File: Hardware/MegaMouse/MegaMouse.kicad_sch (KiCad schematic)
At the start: 7 parts, among them J101 MotorL, J102 MotorR, U101 ATmega328P-A, U102 HDSP-7803

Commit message: Make awesome
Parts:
- removed J101: MotorL, MegaMouse:MicroMotor, symbol Connector:Conn_01x05_Female
- removed J102: MotorR, MegaMouse:MicroMotor, symbol Connector:Conn_01x05_Female
- added BT102: Cell2, Battery:BatteryHolder_MPD_BH-18650-PC2, symbol Device:Battery_Cell
- BT101: value Battery_Cell -> Cell1
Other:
- added sheet LeftMotor (motor.kicad_sch)
- added sheet RightMotor (motor.kicad_sch)
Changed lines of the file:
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@@
       (effects (font (size 1.27 1.27)) (justify left))
     )
-    (property "Value" "Battery_Cell" (id 1) (at 238.76 48.7679 0)
+    (property "Value" "Cell1" (id 1) (at 238.76 48.7679 0)
       (effects (font (size 1.27 1.27)) (justify left))
     )
@@
     (pin "3")
   )
-  (symbol (lib_id "Connector:Conn_01x05_Female") (at 205.74 85.725 0) (unit 1)
-    (in_bom yes) (on_board yes) (fields_autoplaced)
-    (property "Reference" "J101" (id 0) (at 207.01 84.4549 0)
-      (effects (font (size 1.27 1.27)) (justify left))
-    )
-    (property "Value" "MotorL" (id 1) (at 207.01 86.9949 0)
-      (effects (font (size 1.27 1.27)) (justify left))
-    )
-    (property "Footprint" "MegaMouse:MicroMotor" (id 2) (at 205.74 85.725 0)
-      (effects (font (size 1.27 1.27)) hide)
-    )
-    (property "Datasheet" "~" (id 3) (at 205.74 85.725 0)
-      (effects (font (size 1.27 1.27)) hide)
-    )
-    (pin "1")
-    (pin "2")
-    (pin "3")
-    (pin "4")
-    (pin "5")
-  )
   (symbol (lib_id "Device:LED_Dual_AAK") (at 43.815 74.93 0) (unit 1)
     (in_bom yes) (on_board yes) (fields_autoplaced)
@@
     (pin "3")
   )
-  (symbol (lib_id "Connector:Conn_01x05_Female") (at 222.25 85.725 0) (unit 1)
-    (in_bom yes) (on_board yes) (fields_autoplaced)
-    (property "Reference" "J102" (id 0) (at 223.52 84.4549 0)
-      (effects (font (size 1.27 1.27)) (justify left))
-    )
-    (property "Value" "MotorR" (id 1) (at 223.52 86.9949 0)
-      (effects (font (size 1.27 1.27)) (justify left))
-    )
-    (property "Footprint" "MegaMouse:MicroMotor" (id 2) (at 222.25 85.725 0)
-      (effects (font (size 1.27 1.27)) hide)
-    )
-    (property "Datasheet" "~" (id 3) (at 222.25 85.725 0)
-      (effects (font (size 1.27 1.27)) hide)
-    )
-    (pin "1")
-    (pin "2")
-    (pin "3")
-    (pin "4")
-    (pin "5")
+  (symbol (lib_id "Device:Battery_Cell") (at 250.19 49.53 0) (unit 1)
+    (in_bom yes) (on_board yes) (fields_autoplaced)
+    (property "Reference" "BT102" (id 0) (at 254 46.2279 0)
+      (effects (font (size 1.27 1.27)) (justify left))
+    )
+    (property "Value" "Cell2" (id 1) (at 254 48.7679 0)
+      (effects (font (size 1.27 1.27)) (justify left))
+    )
+    (property "Footprint" "Battery:BatteryHolder_MPD_BH-18650-PC2" (id 2) (at 250.19 48.006 90)
+      (effects (font (size 1.27 1.27)) hide)
+    )
+    (property "Datasheet" "~" (id 3) (at 250.19 48.006 90)
+      (effects (font (size 1.27 1.27)) hide)
+    )
+    (pin "1")
+    (pin "2")
+  )
+  (sheet (at 245.745 60.325) (size 33.02 19.05) (fields_autoplaced)
+    (stroke (width 0.1524) (type solid) (color 0 0 0 0))
+    (fill (color 0 0 0 0.0000))
+    (property "Sheet name" "LeftMotor" (id 0) (at 245.745 59.6134 0)
+      (effects (font (size 1.27 1.27)) (justify left bottom))
+    )
+    (property "Sheet file" "motor.kicad_sch" (id 1) (at 245.745 79.9596 0)
+      (effects (font (size 1.27 1.27)) (justify left top))
+    )
+  )
+  (sheet (at 245.745 87.63) (size 33.02 19.05) (fields_autoplaced)
+    (stroke (width 0.1524) (type solid) (color 0 0 0 0))
+    (fill (color 0 0 0 0.0000))
+    (property "Sheet name" "RightMotor" (id 0) (at 245.745 86.9184 0)
+      (effects (font (size 1.27 1.27)) (justify left bottom))
+    )
+    (property "Sheet file" "motor.kicad_sch" (id 1) (at 245.745 107.2646 0)
+      (effects (font (size 1.27 1.27)) (justify left top))
+    )
   )
   (sheet_instances
     (path "/" (page "1"))
+    (path "/cab2ae08-2794-43d3-b90a-39adfeeefd96" (page "2"))
+    (path "/f3134389-3b86-403d-ae8e-c46efd53e738" (page "3"))
   )
   (symbol_instances
@@
       (reference "#PWR0101") (unit 1) (value "GND") (footprint "")
     )
+    (path "/cab2ae08-2794-43d3-b90a-39adfeeefd96/30939476-66e6-4fc1-980c-82ef7e0fb2a1"
+      (reference "#PWR0102") (unit 1) (value "GND") (footprint "")
+    )
+    (path "/cab2ae08-2794-43d3-b90a-39adfeeefd96/1459ec6e-ec07-4a49-921b-662925b52015"
+      (reference "#PWR0103") (unit 1) (value "GND") (footprint "")
+    )
+    (path "/cab2ae08-2794-43d3-b90a-39adfeeefd96/4f63fd2b-66dc-4283-9050-d0dcbca9f9c1"
+      (reference "#PWR0104") (unit 1) (value "+5V") (footprint "")
+    )
+    (path "/f3134389-3b86-403d-ae8e-c46efd53e738/30939476-66e6-4fc1-980c-82ef7e0fb2a1"
+      (reference "#PWR0105") (unit 1) (value "GND") (footprint "")
+    )
+    (path "/f3134389-3b86-403d-ae8e-c46efd53e738/1459ec6e-ec07-4a49-921b-662925b52015"
+      (reference "#PWR0106") (unit 1) (value "GND") (footprint "")
+    )
+    (path "/f3134389-3b86-403d-ae8e-c46efd53e738/4f63fd2b-66dc-4283-9050-d0dcbca9f9c1"
+      (reference "#PWR0107") (unit 1) (value "+5V") (footprint "")
+    )
+    (path "/cab2ae08-2794-43d3-b90a-39adfeeefd96/5a437b24-3dcb-4ae5-ae24-39aa4ab2bf13"
+      (reference "#PWR0108") (unit 1) (value "+5V") (footprint "")
+    )
+    (path "/cab2ae08-2794-43d3-b90a-39adfeeefd96/d7e3ad90-6f75-4218-911d-167200c667a7"
+      (reference "#PWR0109") (unit 1) (value "GND") (footprint "")
+    )
+    (path "/cab2ae08-2794-43d3-b90a-39adfeeefd96/40b57512-351e-4018-b8d3-8fa2b34fe0da"
+      (reference "#PWR0110") (unit 1) (value "+5V") (footprint "")
+    )
+    (path "/f3134389-3b86-403d-ae8e-c46efd53e738/5a437b24-3dcb-4ae5-ae24-39aa4ab2bf13"
+      (reference "#PWR0111") (unit 1) (value "+5V") (footprint "")
+    )
+    (path "/f3134389-3b86-403d-ae8e-c46efd53e738/d7e3ad90-6f75-4218-911d-167200c667a7"
+      (reference "#PWR0112") (unit 1) (value "GND") (footprint "")
+    )
+    (path "/f3134389-3b86-403d-ae8e-c46efd53e738/40b57512-351e-4018-b8d3-8fa2b34fe0da"
+      (reference "#PWR0113") (unit 1) (value "+5V") (footprint "")
+    )
     (path "/3108476a-847a-4adf-becb-69126938c9dd"
-      (reference "BT101") (unit 1) (value "Battery_Cell") (footprint "Battery:BatteryHolder_MPD_BH-18650-PC2")
+      (reference "BT101") (unit 1) (value "Cell1") (footprint "Battery:BatteryHolder_MPD_BH-18650-PC2")
+    )
+    (path "/ecd548c5-d6f5-4492-9620-aefa337bb394"
+      (reference "BT102") (unit 1) (value "Cell2") (footprint "Battery:BatteryHolder_MPD_BH-18650-PC2")
+    )
+    (path "/cab2ae08-2794-43d3-b90a-39adfeeefd96/efe86208-243a-43d8-bd2e-7eeede0585cd"
+      (reference "C201") (unit 1) (value "10uf") (footprint "Capacitor_SMD:CP_Elec_4x3")
+    )
+    (path "/f3134389-3b86-403d-ae8e-c46efd53e738/efe86208-243a-43d8-bd2e-7eeede0585cd"
+      (reference "C301") (unit 1) (value "10uf") (footprint "Capacitor_SMD:CP_Elec_4x3")
     )
     (path "/ca9b22a2-b92f-47fd-a808-1f1f393a3eb7"
@@
       (reference "D102") (unit 1) (value "RightTail") (footprint "MegaMouse:BrakeLight")
     )
-    (path "/bd1226fe-f6ac-4ec8-9650-08c99a4f03a9"
-      (reference "J101") (unit 1) (value "MotorL") (footprint "MegaMouse:MicroMotor")
-    )
-    (path "/e73cdaaa-7743-4e85-b32f-0823784545c7"
-      (reference "J102") (unit 1) (value "MotorR") (footprint "MegaMouse:MicroMotor")
+    (path "/cab2ae08-2794-43d3-b90a-39adfeeefd96/baf2f694-5d21-4a5a-b7c3-f601a15715f0"
+      (reference "J201") (unit 1) (value "Motor") (footprint "MegaMouse:MicroMotor")
+    )
+    (path "/f3134389-3b86-403d-ae8e-c46efd53e738/baf2f694-5d21-4a5a-b7c3-f601a15715f0"
+      (reference "J301") (unit 1) (value "Motor") (footprint "MegaMouse:MicroMotor")
     )
     (path "/6237422b-5d80-4047-94aa-94384be9ec54"
@@
       (reference "U102") (unit 1) (value "HDSP-7803") (footprint "Display_7Segment:HDSP-7801")
     )
-  )
+    (path "/cab2ae08-2794-43d3-b90a-39adfeeefd96/4c257885-dae9-4de1-8723-d1220bd3380a"
+      (reference "U201") (unit 1) (value "DRV8871DDA") (footprint "Package_SO:Texas_HTSOP-8-1EP_3.9x4.9mm_P1.27mm_EP2.95x4.9mm_Mask2.4x3.1mm_ThermalVias")
+    )
+    (path "/f3134389-3b86-403d-ae8e-c46efd53e738/4c257885-dae9-4de1-8723-d1220bd3380a"
+      (reference "U301") (unit 1) (value "DRV8871DDA") (footprint "Package_SO:Texas_HTSOP-8-1EP_3.9x4.9mm_P1.27mm_EP2.95x4.9mm_Mask2.4x3.1mm_ThermalVias")
+    )
+  )

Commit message: Clean board
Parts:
- U102: value HDSP-7803 -> STATE
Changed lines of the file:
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@@
   )
   (symbol (lib_id "Display_Character:HDSP-7803") (at 34.925 34.925 0) (unit 1)
-    (in_bom yes) (on_board yes) (fields_autoplaced)
-    (property "Reference" "U102" (id 0) (at 34.925 16.51 0))
-    (property "Value" "HDSP-7803" (id 1) (at 34.925 19.05 0))
+    (in_bom yes) (on_board yes)
+    (property "Reference" "U102" (id 0) (at 34.925 20.955 0))
+    (property "Value" "STATE" (id 1) (at 34.925 48.895 0))
     (property "Footprint" "Display_7Segment:HDSP-7801" (id 2) (at 34.925 48.895 0)
       (effects (font (size 1.27 1.27)) hide)
@@
     )
     (path "/07d9b08c-1968-419d-8cab-af1700401c87"
-      (reference "U102") (unit 1) (value "HDSP-7803") (footprint "Display_7Segment:HDSP-7801")
+      (reference "U102") (unit 1) (value "STATE") (footprint "Display_7Segment:HDSP-7801")
     )
     (path "/cab2ae08-2794-43d3-b90a-39adfeeefd96/4c257885-dae9-4de1-8723-d1220bd3380a"

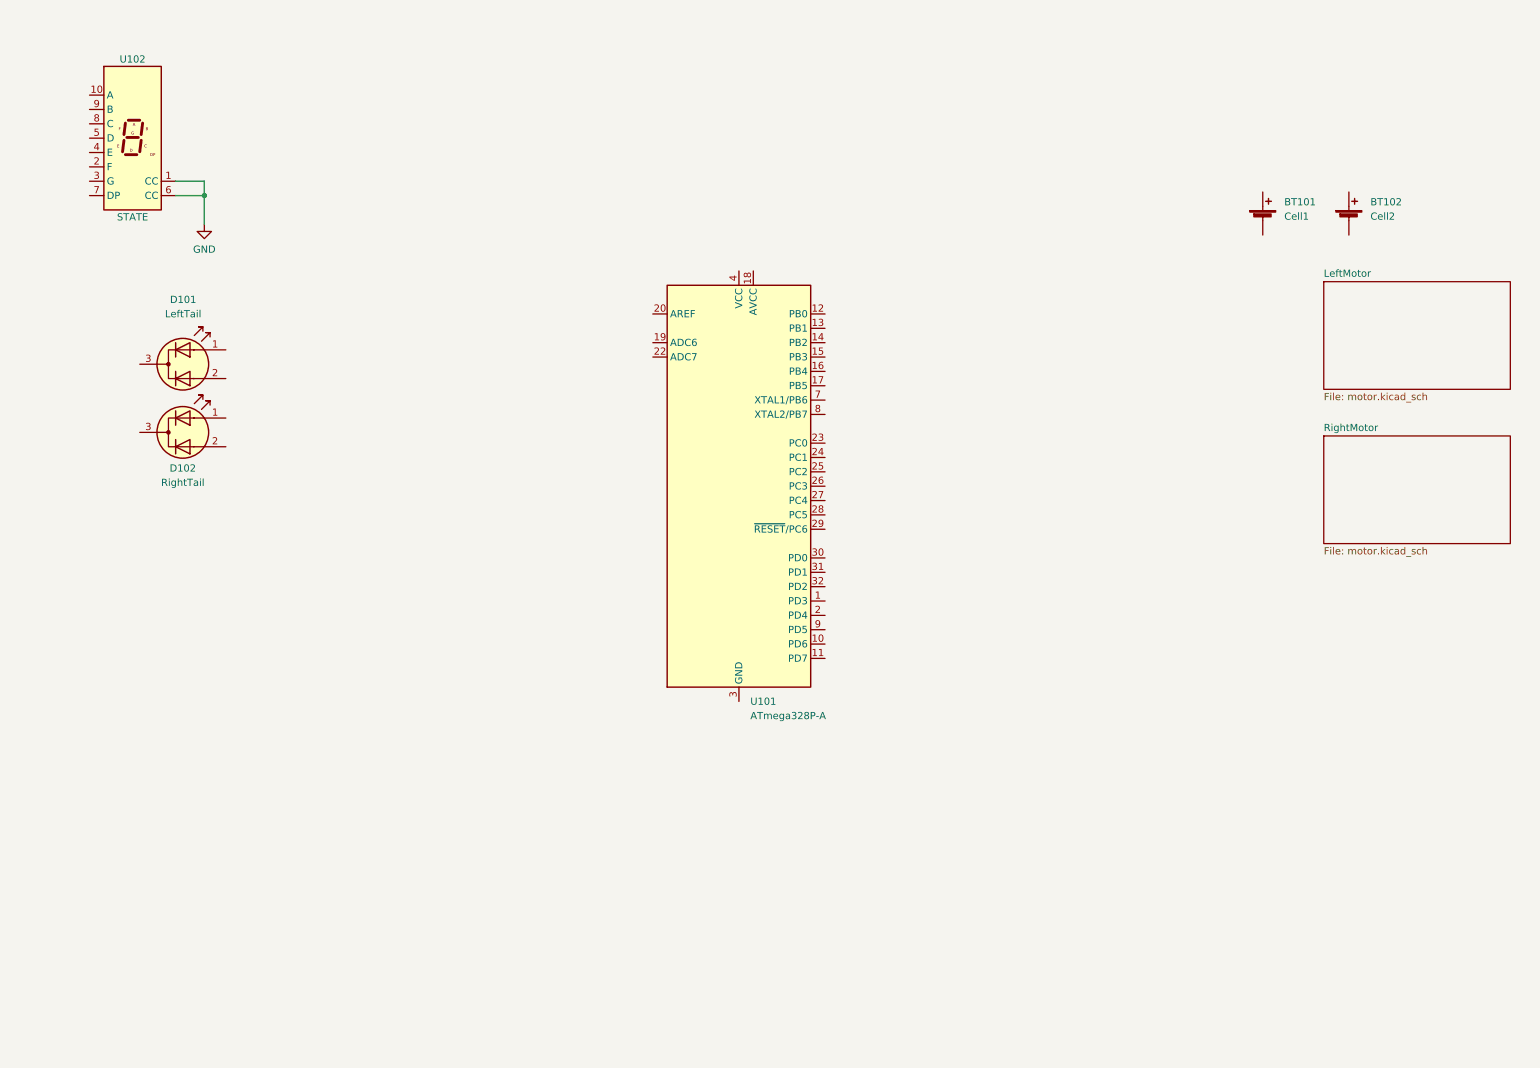
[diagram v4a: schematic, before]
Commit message: Add second layer
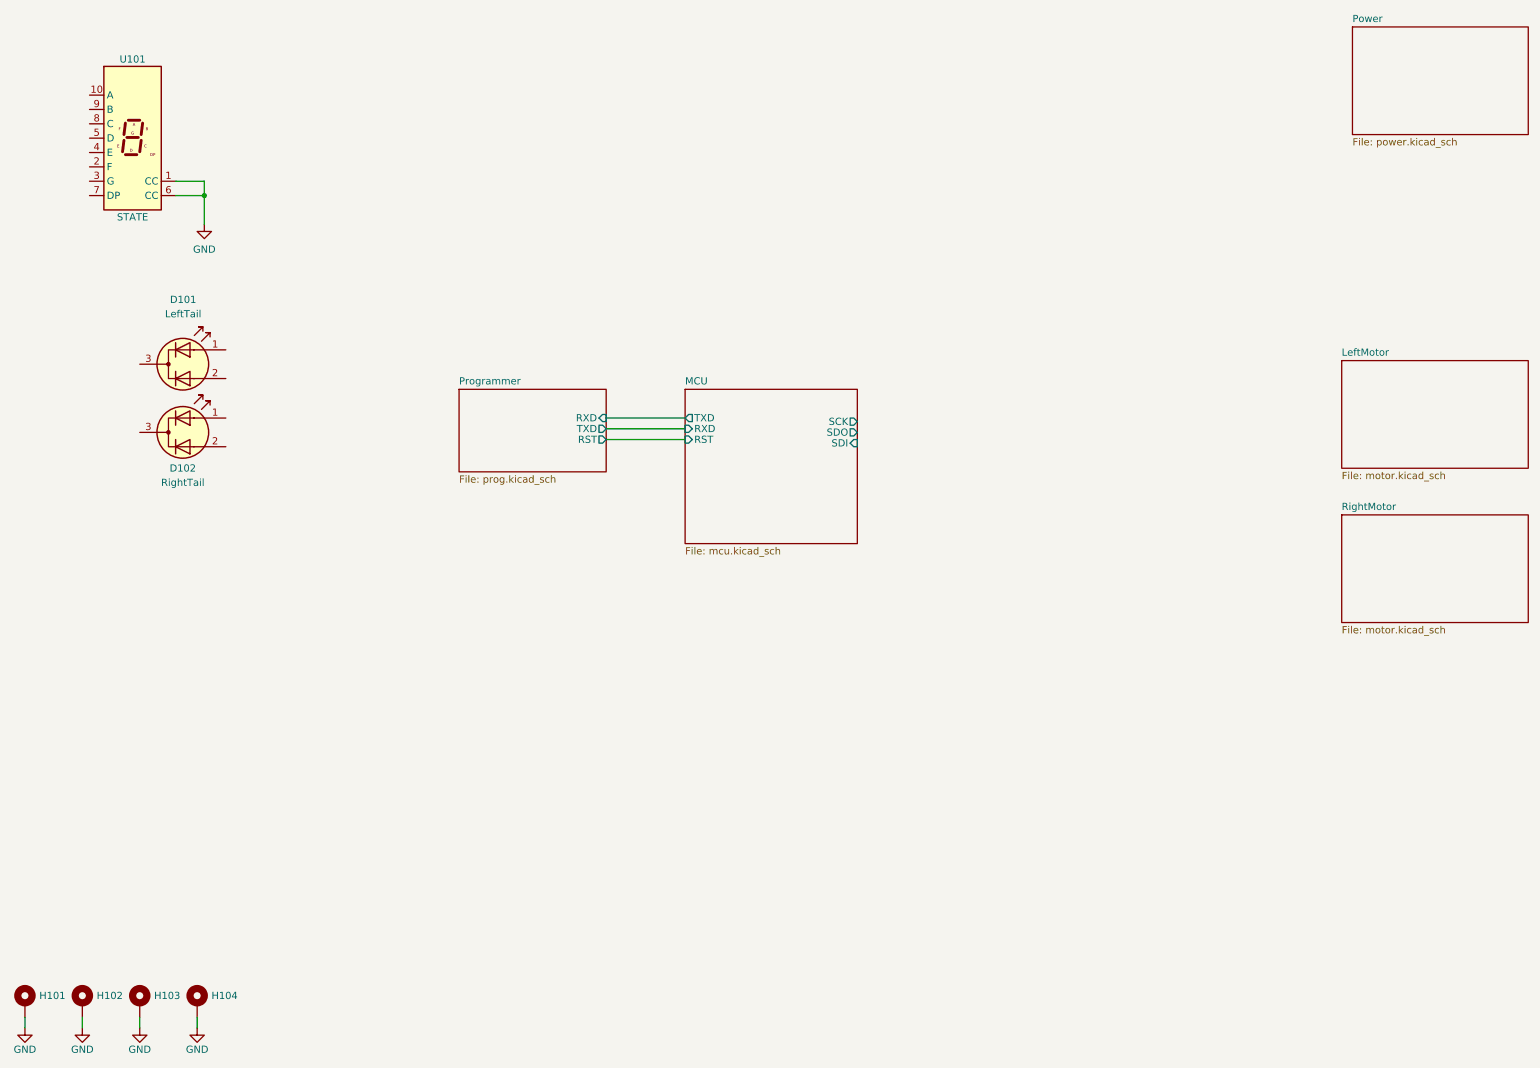
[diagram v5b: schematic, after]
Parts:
- removed BT101: Cell1, Battery:BatteryHolder_MPD_BH-18650-PC2, symbol Device:Battery_Cell
- removed BT102: Cell2, Battery:BatteryHolder_MPD_BH-18650-PC2, symbol Device:Battery_Cell
- removed U101: ATmega328P-A, Package_QFP:TQFP-32_7x7mm_P0.8mm, symbol MCU_Microchip_ATmega:ATmega328P-A
- added H101, H102, H103, H104: MountingHole_Pad, MountingHole:MountingHole_3mm_Pad, symbol Mechanical:MountingHole_Pad
- renumbered U102 to U101
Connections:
- net GND: now also H101.1, H102.1, H103.1, H104.1
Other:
- added sheet MCU (mcu.kicad_sch)
- added sheet Power (power.kicad_sch)
- added sheet Programmer (prog.kicad_sch)

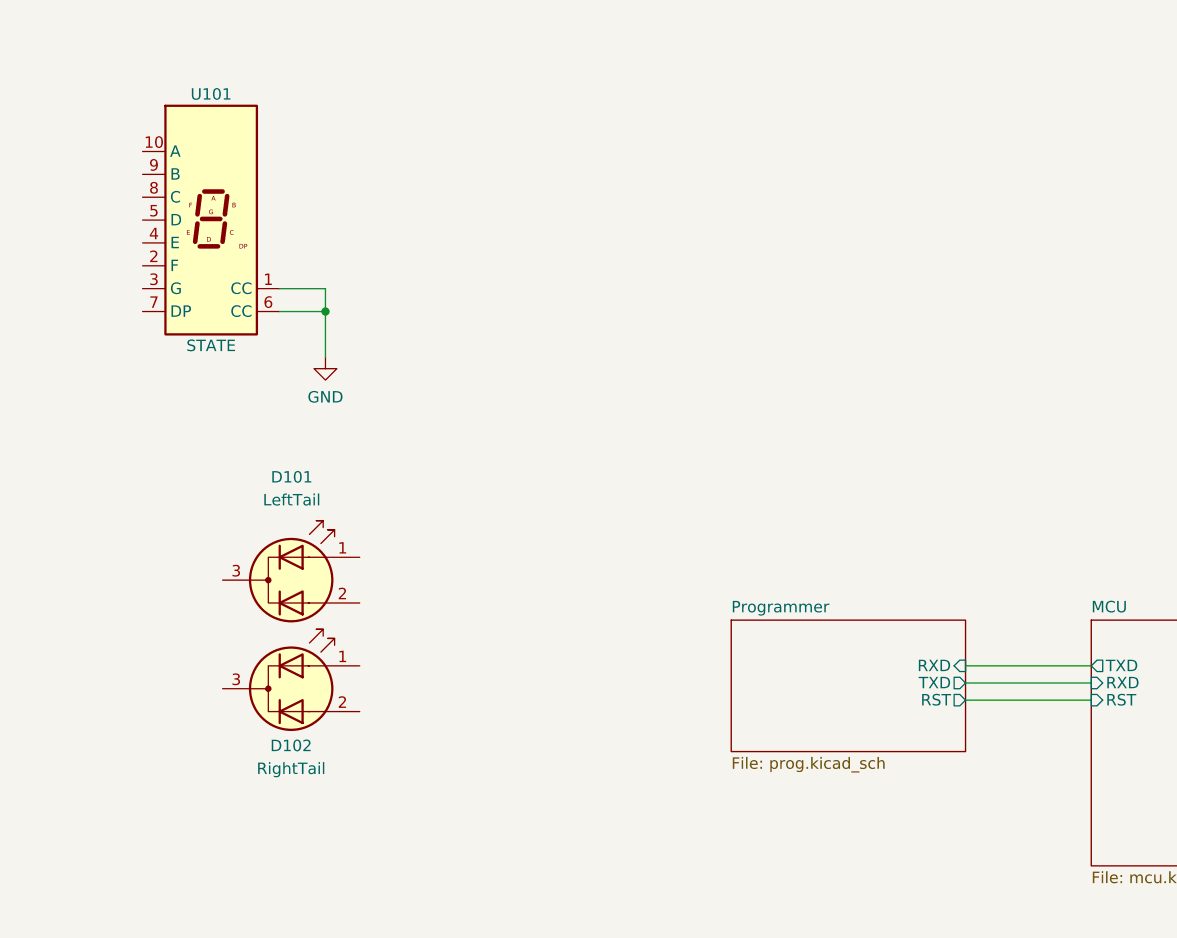
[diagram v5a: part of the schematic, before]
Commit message: move upper body
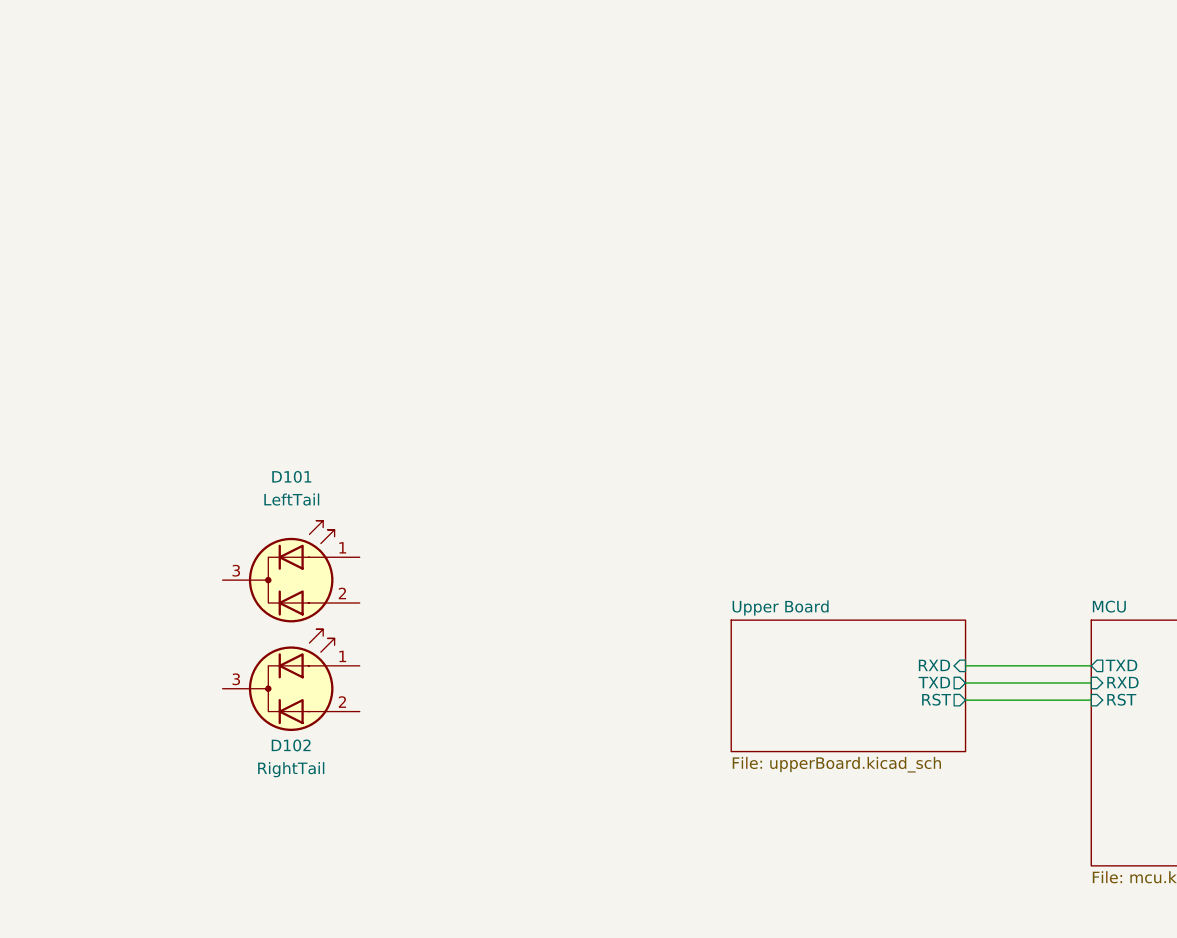
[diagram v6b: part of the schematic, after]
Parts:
- removed U101: STATE, Display_7Segment:HDSP-7801, symbol Display_Character:HDSP-7803
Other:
- sheet Programmer renamed Upper Board
- sheet Upper Board: file prog.kicad_sch -> upperBoard.kicad_sch
